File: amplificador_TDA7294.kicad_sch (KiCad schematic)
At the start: 13 parts, among them U1 TDA7294

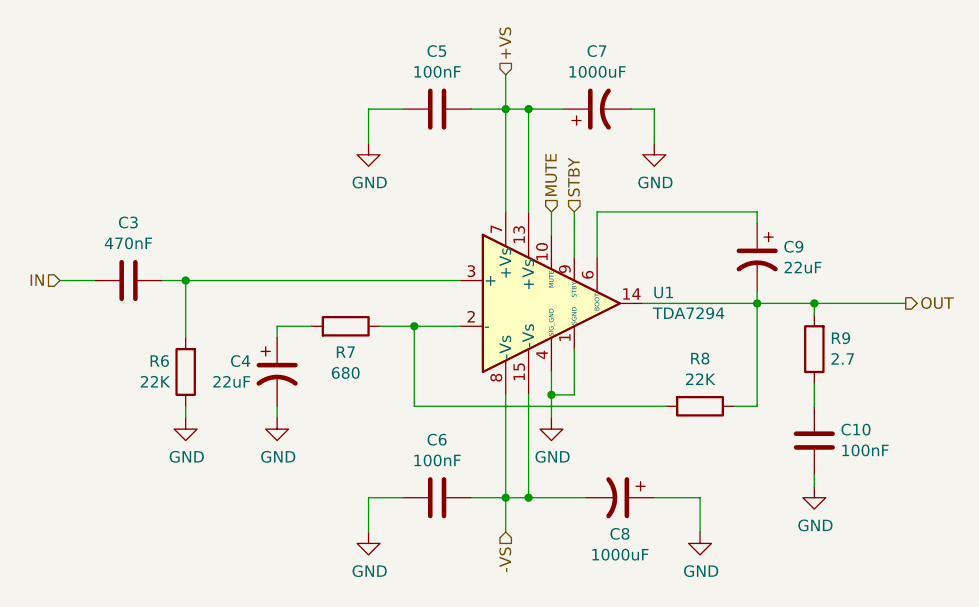
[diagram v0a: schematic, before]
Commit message: add version puenteable y archivos en pdf
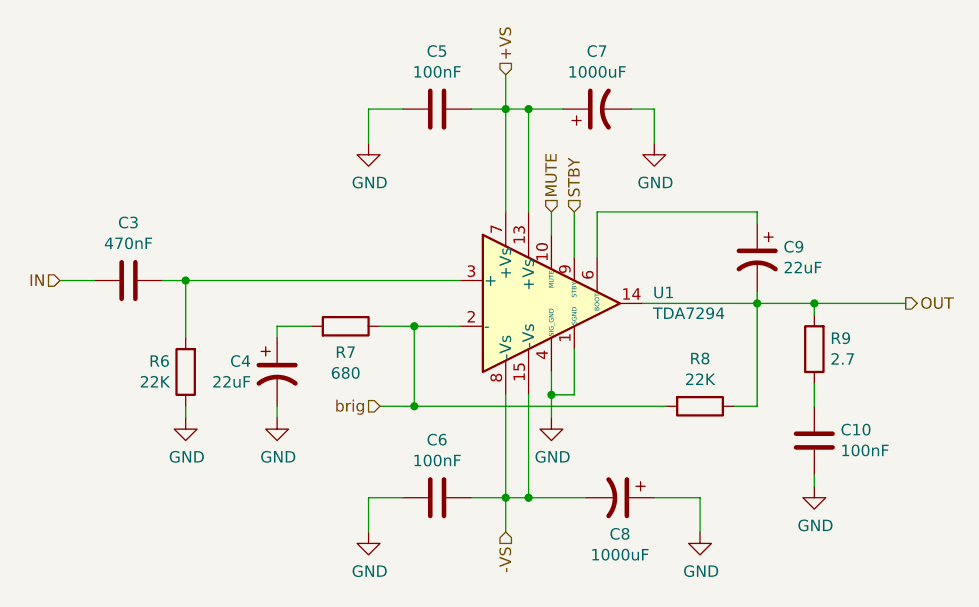
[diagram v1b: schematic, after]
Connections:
- net brig: now reaches R7.1, R8.2, U1.2 (-)
